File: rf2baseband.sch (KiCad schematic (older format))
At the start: 20 parts, among them U701 TLV4172

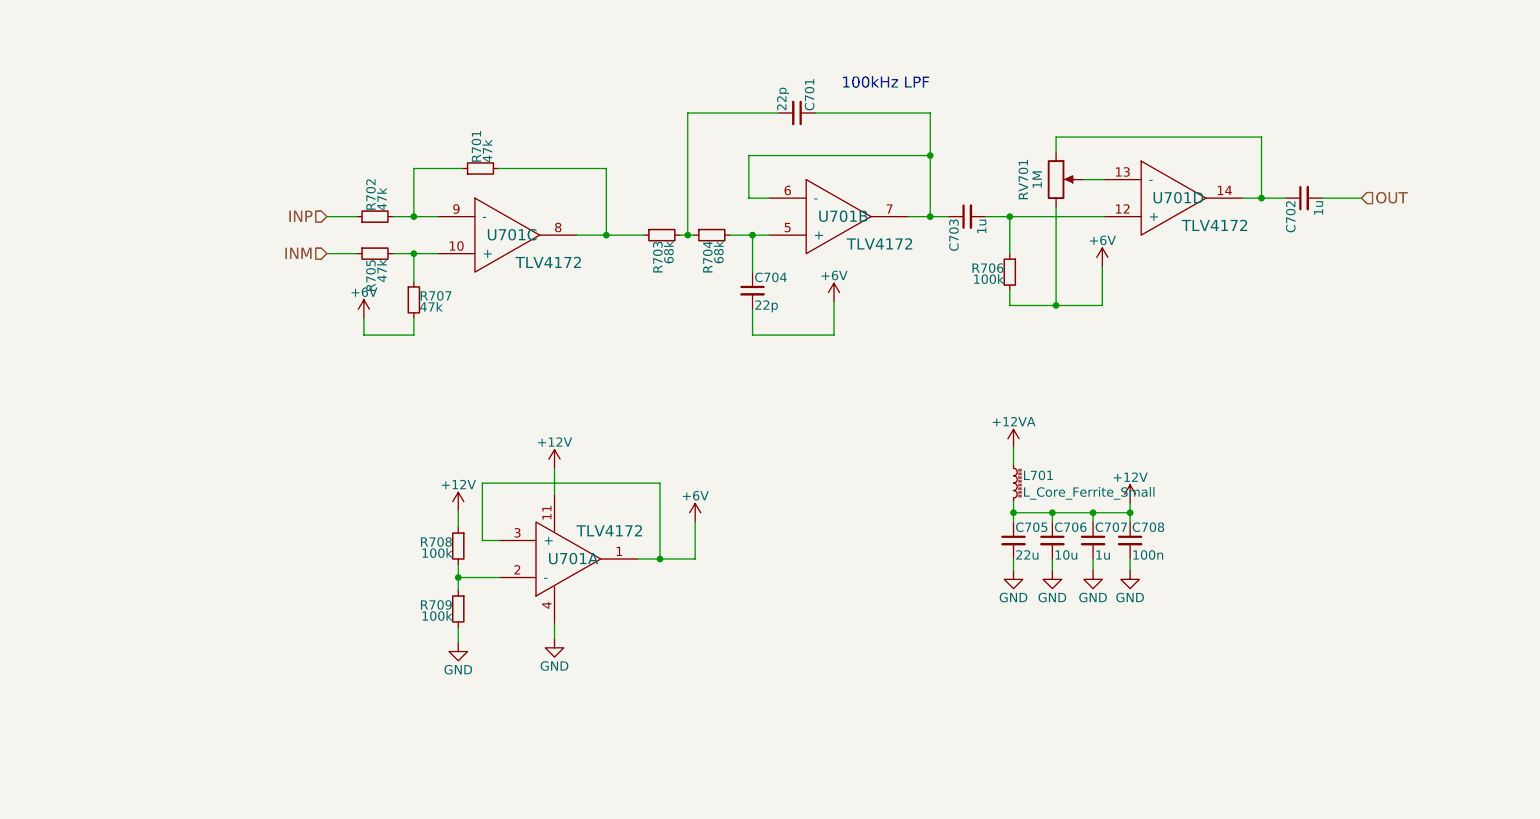
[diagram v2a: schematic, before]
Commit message: Finished circuit layout (for the RF board)
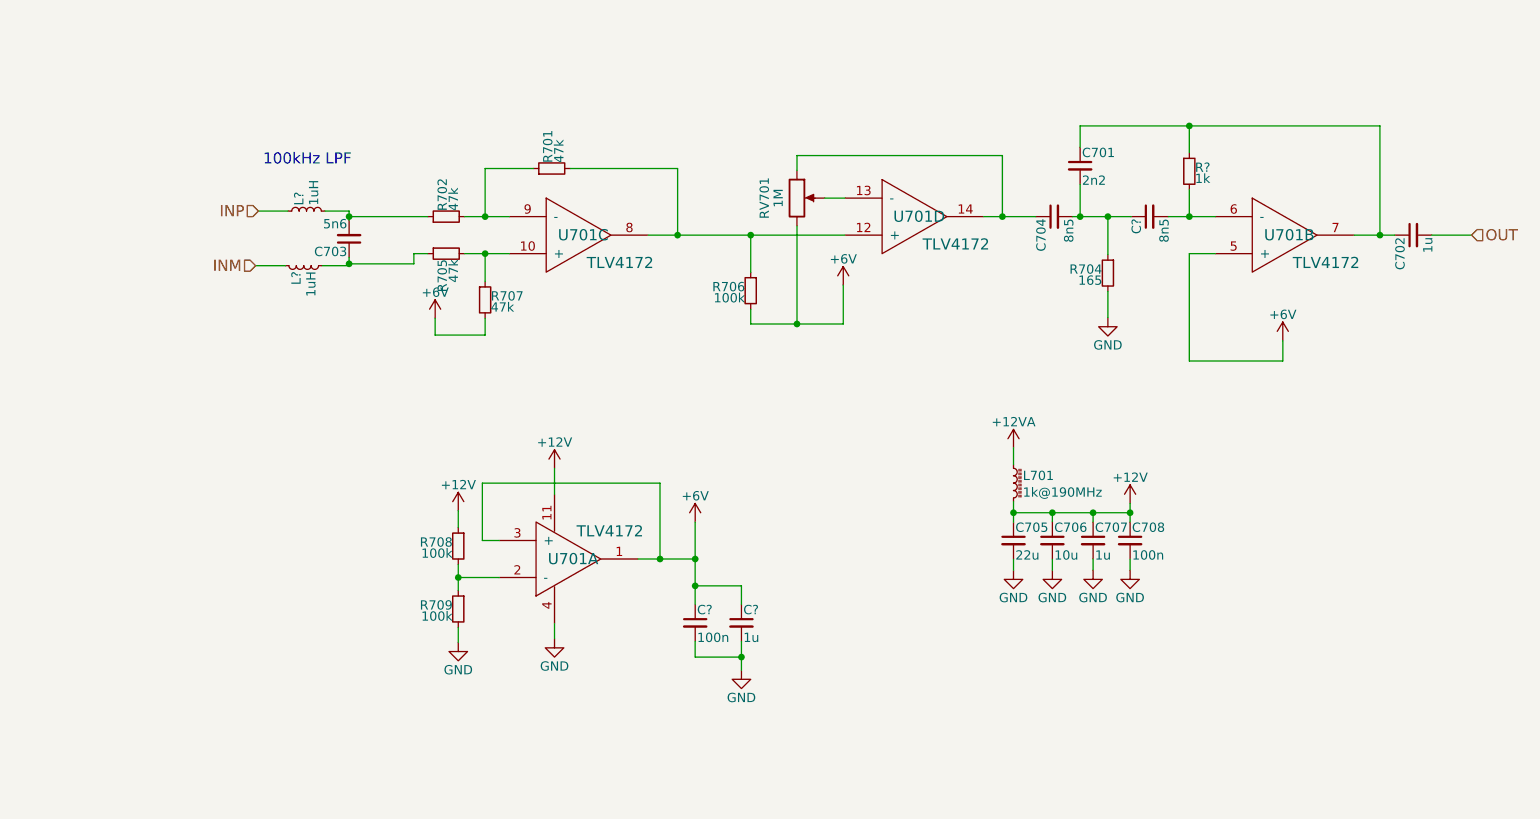
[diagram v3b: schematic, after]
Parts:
- removed R703: 68k, Resistors_SMD:R_1206_HandSoldering, symbol R_Small
- added C?: 8n5, Capacitors_SMD:C_0603_HandSoldering, symbol C_Small
- added C?: 100n, Capacitors_SMD:C_0603_HandSoldering, symbol C_Small
- added C?: 1u, Capacitors_SMD:C_0603_HandSoldering, symbol C_Small
- added L? (x2): 1uH, symbol L_Small
- added R?: 1k, Resistors_SMD:R_1206_HandSoldering, symbol R_Small
- C701: value 22p -> 2n2
- C703: value 1u -> 5n6
- C704: value 22p -> 8n5
- L701: value L_Core_Ferrite_Small -> 1k@190MHz; footprint (none) -> Capacitors_SMD:C_0402
- R704: value 68k -> 165
- RV701: footprint (none) -> rajsradar:Bourns-3362P
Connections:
- net +6V: now also U701.5 (+), C?.1, C?.1; no longer C704.2
- net GND: now also R704.2, C?.2, C?.2
- net INM: now also L?.1; no longer R705.1
- net INP: now also L?.1; no longer R702.1
- net OUT: no longer C702.2
- net at R706.1, U701.12 (+): now also R701.2, U701.8; no longer C703.2
- net at RV701.1, U701.14: now also C704.1; no longer C702.1
- net at C701.1, U701.7: now also C702.1, R?.1; no longer C703.1, U701.6 (-)
- net at C701.2, R704.1: now also C704.2, C?.1
- new net: C?.2, R?.2, U701.6 (-)
- new net: C703.2, L?.2, R702.1
- new net: C703.1, L?.2, R705.1
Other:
- moved on the sheet: C701, C702, C703, C704, R701, R702, R704, R705, R706, R707, RV701, U701B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

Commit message: Switch signal conditioning to fully differential
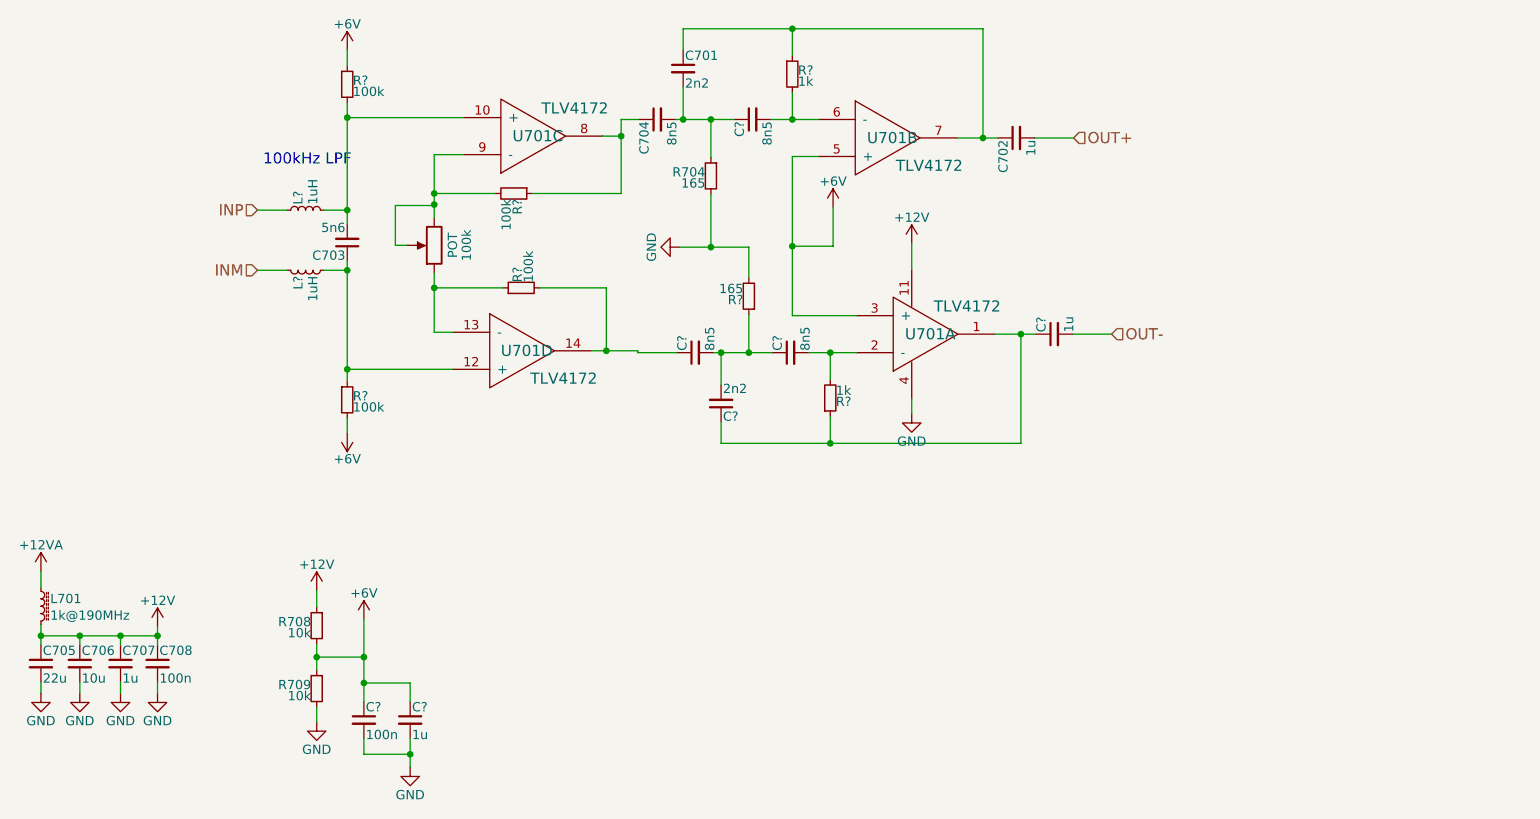
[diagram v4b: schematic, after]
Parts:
- removed R701, R702, R705, R707: 47k, Resistors_SMD:R_0603_HandSoldering, symbol R_Small
- removed R706: 100k, Resistors_SMD:R_0402, symbol R_Small
- removed RV701: 1M, rajsradar:Bourns-3362P, symbol POT
- added 100k: POT, symbol POT
- added C? (x2): 8n5, Capacitors_SMD:C_0603_HandSoldering, symbol C_Small
- added C?: 2n2, Capacitors_SMD:C_0603_HandSoldering, symbol C_Small
- added C?: 1u, Capacitors_SMD:C_0603_HandSoldering, symbol C_Small
- added R? (x4): 100k, symbol R_Small
- added R?: 165, Resistors_SMD:R_1206_HandSoldering, symbol R_Small
- added R?: 1k, Resistors_SMD:R_1206_HandSoldering, symbol R_Small
- R708, R709: value 100k -> 10k
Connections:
- net +6V: now also R708.2, R709.1, R?.1, R?.2; no longer U701.1
- net GND: now also R?.2
- net at U701.12 (+): now also C703.1, L?.2, R?.1; no longer U701.8
- net at U701.13 (-): now also 100k.1, R?.1
- net at U701.14: now also C?.1, R?.2; no longer C704.1
- net at U701.10 (+): now also C703.2, L?.2, R?.2
- net at U701.9 (-): now also 100k.3, R?.2
- net OUT+: now reaches C702.2
- new net: C704.1, R?.1, U701.8
- new net: C?.1, C?.1, R?.1, U701.1
- new net: C?.2, R?.2, U701.2 (-)
- new net: C?.1, C?.2, C?.2, R?.1
- new net OUT-: C?.2
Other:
- moved on the sheet: C701, C702, C703, C704, C705, C706, C707, C708, C?, L701, L?, R704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
